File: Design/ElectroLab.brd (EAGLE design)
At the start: 175 x 100 mm, 232 parts, among them IC1 LM2902DT, IC10 CD4511BNSR, IC11 PAM8403, IC13 ADXL337, IC14 MIC5205, IC2 LM2902DT, IC3 SN74LV08ADR, IC4 SN74LV32ADR, IC5 SN74LV04ADR, IC6 4027D, IC7 4027D, IC8 NE555D, U1 USB, U2 GAS_SENSOR

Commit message: Updated V3R1
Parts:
- removed AR1, AR2, AR3, AR4: 1K, SpaceDIY:RESISTOR_ARRAY_X8_CAY17
- removed C33, C34: 10uF, SpaceDIY_passive_components:0603
- removed D1, D2, D3, D4: (no value), Seeed-OPL-Diode:LED-1206
- removed DP1: 2X7_SEGMENT_COMMON_CATODE_12_PINS, SpaceDIY:2X7_SEGMENT_COMMON_CATODE_12_PINS
- removed IC1, IC2: LM2902DT, Texas Instruments_By_element14_Batch_1:SOIC127P600X175-14N
- removed IC10: CD4511BNSR, SpaceDIY:SN74LS247D
- removed IC5: SN74LV04ADR, Texas Instruments_By_element14_Batch_1:SOIC127P600X175-14N
- removed JC1, JC2: SWTCHCRFT_3.5JACK5-JACK-SMD, jmsaavedra:4-JACK-SMD
- removed L0, L1, L2, L3, L4, L5, L6, L7: (no value), adafruit:1206
- removed L10, L17, L8, L9: Grn, adafruit:1206
- removed L11, L12, L13: Ylw, adafruit:1206
- removed L14, L15, L16: Red, adafruit:1206
- removed LDR: (no value), photo-elements:TO-5_V10
- removed LED_: (no value), SpaceDIY_passive_components:PLCC-6
- removed PB1, PB2, PB3, PB4, PB5, PB6, PB7, PB8, PB9: (no value), Seeed-OPL-Switch:SW4-SMD-6.0X6.0X5.0MM
- removed PH10, PH2, PH21, PH3, PH4, PH5, PH6, PH7, PH8, PH9: (no value), pinhead:1X02
- removed PH11, PH14, PH15, PH16, PH17, PH18, PH19, PH20, PH22, PH23, PH24, PH25, PH26, PH27, PH28, PH29, PH30, PH38, PH64: (no value), pinhead:1X03
- removed PH31, PH58, PH59, PH60, PH61, PH62: (no value), pinhead:1X30
- removed PH32, PH33, PH35, PH36, PH37, PH65: (no value), pinhead:1X04
- removed PH34: (no value), pinhead:1X01
- removed PH39, PH40: (no value), pinhead:1X06
- removed PH41: (no value), pinhead:2X07
- removed PH42, PH43, PH44, PH45, PH46: (no value), pinhead:1X08
- removed PH47: (no value), pinhead:1X09
- removed PH48, PH49, PH50, PH51, PH52, PH53, PH54, PH55, PH56, PH57: (no value), adafruit:1X10-BIG
- removed PH63: (no value), con-lstb:MA08-2
- added ARR1, ARR2, ARR3, ARR4, ARR5, ARR6, ARR7: 4_RES_ARRAY_R06031KOHM, SpaceDIY_passive_components:0603-ARC
- added C28, C37, C38, C39: 10uF, rcl:C0603
- added D5, D6, D7, D8: LL4148, SpaceDIY_semiconductors:LL-34
- added IC15: 74HC32S14-13, SpaceDIY_IC:SO14
- added IC9: TP4056, TP4056:SOT23-8
- added J1: (no value), SpaceDIY_connectors:JST-2-SMD
- added J10, J11, J12, J2, J4, J5, J6, J7, J8, J9: (no value), SpaceDIY_connectors:1X10
- added J13: AUDIO_JACK_MONO_3.5LCSC, SpaceDIY_connectors:PJ316
- added J14, J15, J16, J17, J18, J19: (no value), SpaceDIY_connectors:1X30
- added J20, J21, J22, J23, J24, J25, J26, J27, J28, J29, J30, J31, J32, J33, J34, J35, J36, J37: (no value), SpaceDIY_connectors:1X03
- added J3, J43, J44, J52, J53, J55: (no value), SpaceDIY_connectors:1X04
- added J38, J39, J40, J41, J47, J48, J49, J50, J54: (no value), SpaceDIY_connectors:1X02
- added J42, J51: (no value), SpaceDIY_connectors:1X01
- added J45, J46: (no value), SpaceDIY_connectors:1X06
- added J56: (no value), SpaceDIY_connectors:1X09
- added LED1, LED10, LED11, LED12, LED13, LED2, LED3, LED4, LED5, LED6, LED7, LED8, LED9: E6CC1205RYGC2UDA, SpaceDIY_semiconductors:BICOLOR_LED
- added RGB: CLEAR, SpaceDIY_semiconductors:LED-RGB-THRU
- added S10, S2, S3, S4, S5, S6, S7, S8, S9: MOMENTARY-SWITCH-SPST-PTH-6.0MM, SparkFun-Switches:TACTILE_SWITCH_PTH_6.0MM
- added U$1: FJ5101AG, SpaceDIY_semiconductors:7-SEGMENT
- added U$2, U$3, U$4, U$5, U$6: CONN_08, SpaceDIY_connectors:1X08
- added U$7: CD4511BNSR, SpaceDIY_IC:SO16
- added U3: AMS1117-3.3VSMD, SpaceDIY_IC:SOT223
- added X8: USB-C-POWER, SpaceDIY_connectors:USB-C-POWER
- C1, C10, C11, C12, C13, C14, C15, C16, C2, C3, C4, C5, C6, C7, C8, C9: device resistor:C1206 -> SpaceDIY_passive_components:0603
- C17, C18: device rcl:A/3216-18R -> SpaceDIY_passive_components:B/3528-21R
- C19, C20, C35, C36: device rcl:D/7343-31R -> SpaceDIY_passive_components:D/7343-31R
- C27: device rcl:D/7343-31W -> SpaceDIY_passive_components:D/7343-31R
- C29, C30, C31: value 10nF -> 0.1uF
- C32: value 100nF -> 0.1uF
- H1, H2, H3, H4: value (none) -> MOUNT-PAD-ROUND2.8
- IC13: value ADXL337 -> 74HC08DD; device SpaceDIY_IC:LFCSP-3X3 -> SpaceDIY_IC:SO14
- IC14: value MIC5205 -> 74HC04DD; device SparkFun:SOT23-5 -> SpaceDIY_IC:SO14
- IC3: value SN74LV08ADR -> LM324DTD; device Texas Instruments_By_element14_Batch_1:SOIC127P600X175-14N -> SpaceDIY_IC:SO14
- IC4: value SN74LV32ADR -> LM324DTD; device Texas Instruments_By_element14_Batch_1:SOIC127P600X175-14N -> SpaceDIY_IC:SO14
- IC6, IC7: value 4027D -> MC74HC112ADR2G; device 40xx:SO16 -> SpaceDIY_IC:SO16
- IC8: value NE555D -> TLC555CDR
- MIC: value ELECTRET_MICROPHON-WM-64PC/64PK -> MICROPHONE; device microphon:WM-64PC/64PK -> SpaceDIY_sensors:MICROPHONE
- NTC: device adafruit:R1206@1 -> SpaceDIY_sensors:NTC
- P1: value (none) -> SLIDE_POT_20MM; device SpaceDIY:SLIDE_POT_20MM -> SpaceDIY_electromechanical:RS201111J011
- PH1: value (none) -> PHOTORESISTOR; device pinhead:1X01 -> SpaceDIY_sensors:GL5516
- PH12: device pinhead:1X03 -> SpaceDIY_connectors:1X03
- R1, R10, R11, R12, R13, R14, R15, R16, R17, R18, R19, R2, R20, R21, R22, R23, R24, R25, R26, R27, R28, R29, R3, R30, R31, R35, R36, R37, R38, R39, R4, R41, R42, R43, R44, R45, R46, R47, R48, R49, R5, R50, R51, R52, R53, R54, R55, R56, R57, R58, R59, R6, R7, R8, R9: device resistor:R1206 -> SpaceDIY_passive_components:0603
- R32: value 330 -> 1.2k; device resistor:R1206 -> rcl:R0603
- R33: value 330 -> 1K; device resistor:R1206 -> SpaceDIY_passive_components:0603
- R34: value 330 -> 1k; device resistor:R1206 -> SpaceDIY_passive_components:0603
- SP1: value 32MM_SPEAKER -> SPEAKERFS1508MB0810-H8.0; device SpaceDIY:32MM_SPEAKER -> SpaceDIY_electromechanical:FS1508MB0810-H8.0
- T1: value (none) -> MMBT2222A; device transistor:SOT23-BEC -> SpaceDIY_semiconductors:SOT23
- T2, T3: value (none) -> T_NPNMMBT2222A-1P_CHANGJ_SOT23-BEC; device transistor:SOT23-BEC -> SpaceDIY_semiconductors:SOT23
- T4, T5: value (none) -> T_PNPMMBT5401_CHANGJ_SOT23-BEC; device transistor:SOT23-BCE -> SpaceDIY_semiconductors:SOT23
- U$16: device SpaceDIY:RESISTIVE_SENSOR_PAD -> SpaceDIY_sensors:RESISTIVE_SENSOR_PAD
- U1: value USB -> ADXL335; device daspilker:FCI-10103594-0001LF -> SparkFun-Sensors:LFCSP-16-4X4
- U2: device SparkFun:MQ-3 -> SpaceDIY_sensors:GAS_SENSOR
- moved U1 112.9 mm to (116.8, 47.0), flipped to the bottom, turned to 0 degrees
- moved PH1 102.9 mm to (73.7, 47.0), turned to 270 degrees
- moved R37 74.5 mm to (89.6, 74.3), turned to 90 degrees
- moved R36 71.6 mm to (86.7, 74.3), turned to 90 degrees
- moved R38 70.0 mm to (82.5, 49.6), turned to 270 degrees
- moved R35 68.9 mm to (83.8, 74.3), turned to 90 degrees
- moved IC14 51.0 mm to (167.5, 50.5), turned to 270 degrees
- moved R34 27.5 mm to (40.9, 92.1)
- moved R33 27.3 mm to (40.9, 95.1)
- moved IC4 26.4 mm to (162.0, 70.5), turned to 180 degrees
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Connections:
- removed net 3.3V: C32.1, C33.1, IC13.14, IC13.15, IC14.5
- removed net D0: PH41.1, PH63.1, R32.2
- removed net D1: PH41.2, PH63.2
- removed net D10: PH41.11, PH63.11, R37.2
- removed net D11: PH41.12, PH63.12
- removed net D12: PH41.13, PH63.13, R38.2
- removed net D13: PH41.14, PH63.14
- removed net D2: PH41.3, PH63.3, R33.2
- removed net D3: PH41.4, PH63.4
- removed net D4: PH41.5, PH63.5, R34.2
- removed net D5: PH41.6, PH63.6
- removed net D6: PH41.7, PH63.7, R35.2
- removed net D7: PH41.8, PH63.8
- removed net D8: PH41.9, PH63.9, R36.2
- removed net D9: PH41.10, PH63.10
- removed net DG1: DP1.9, PH3.1
- removed net DG2: DP1.4, PH3.2
- removed net DP: DP1.2
- removed net JC1: JC1.2, PH12.2
- removed net JC2: JC2.2, PH64.2
- removed net N$121: JC2.3, PH64.1
- removed net N$228: PB1.1, PB1.2, PB2.1, PB2.2, PB3.1, PB3.2, PH19.3
- removed net N$229: PB4.1, PB4.2, PB5.1, PB5.2, PB6.1, PB6.2, PH19.2
- removed net N$230: PB7.1, PB7.2, PB8.1, PB8.2, PB9.1, PB9.2, PH19.1
- removed net N$233: PB3.3, PB3.4, PB6.3, PB6.4, PB9.3, PB9.4, PH20.3
- removed net N$292: L8.A, R48.1
- removed net N$300: L9.A, R49.1
- removed net N$301: L10.A, R50.1
- removed net N$302: L11.A, R51.1
- removed net N$303: L12.A, R52.1
- removed net N$304: L13.A, R53.1
- removed net N$305: L14.A, R54.1
- removed net N$306: L15.A, R55.1
- removed net N$307: L16.A, R56.1
- removed net VEXT: PH63.15, S1.1
- removed net VUSB: S1.3, U1.1
- new net N$182: LED5.1, R49.2
- new net N$185: LED6.1, R50.2
- new net N$204: LED7.1, R51.2
- new net N$214: LED8.1, R52.2
- new net N$215: LED9.1, R53.2
- new net N$216: LED7.4, R35.2
- new net N$246: LED8.4, R36.2
- new net N$247: LED9.4, R37.2
- new net N$248: LED10.4, R54.2
- new net N$251: LED11.4, R55.2
- new net N$252: LED12.4, R56.2
- new net N$253: J20.3, S2.1, S3.1, S4.1
- new net N$258: J20.2, S5.1, S6.1, S7.1
- new net N$260: J21.3, S10.3, S4.3, S7.3
- new net N$261: J20.1, S10.1, S8.1, S9.1
- new net VBAT: C28.1, IC9.5, J1.1, S1.4
- new net VIN: C37.1, IC9.4, IC9.8, LED1.2, LED1.3, R38.2, U2.A1, U2.HA, X8.VBUS
- new net VOUT: C39.1, F1.2, U3.2
- net A1A: now also ARR1.1, IC13.1, U$2.1; no longer AR1.9, IC3.1, PH45.1
- net A1B: now also ARR1.2, IC13.2, U$2.2; no longer AR1.8, IC3.2, PH45.2
- net A1Y: now also IC13.3, J52.1; no longer IC3.3, PH36.1
- net A2A: now also ARR1.3, IC13.4, U$2.3; no longer AR1.7, IC3.4, PH45.3
- net A2B: now also ARR1.4, IC13.5, U$2.4; no longer AR1.6, IC3.5, PH45.4
- net A2Y: now also IC13.6, J52.2; no longer IC3.6, PH36.2
- net A3A: now also ARR2.1, IC13.9, U$2.5; no longer AR1.1, IC3.9, PH45.5
- net A3B: now also ARR2.2, IC13.10, U$2.6; no longer AR1.2, IC3.10, PH45.6
- net A3Y: now also IC13.8, J52.3; no longer IC3.8, PH36.3
- net A4A: now also ARR2.3, IC13.12, U$2.7; no longer AR1.3, IC3.12, PH45.7
- net A4B: now also ARR2.4, IC13.13, U$2.8; no longer AR1.4, IC3.13, PH45.8
- net A4Y: now also IC13.11, J52.4; no longer IC3.11, PH36.4
- net B: now also J37.3; no longer PH11.3
- net G: now also J37.2, R58.2; no longer PH11.2, R57.2
- net GND: now also ARR1.5, ARR1.6, ARR1.7, ARR1.8, ARR2.5, ARR2.6, ARR2.7, ARR2.8, ARR3.5, ARR3.6, ARR3.7, ARR3.8, ARR4.5, ARR4.6, ARR4.7, ARR4.8, ARR5.5, ARR5.6, ARR5.7, ARR5.8, ARR6.7, ARR6.8, ARR7.5, ARR7.6, ARR7.7, ARR7.8, C28.2, C37.2, C38.2, C39.2, IC14.7, IC15.7, IC3.11, IC4.11, IC6.10, IC6.14, IC6.15, IC7.10, IC7.14, IC7.15, IC9.1, IC9.3, J1.2, J14.1, J14.10, J14.11, J14.12, J14.13, J14.14, J14.15, J14.16, J14.17, J14.18, J14.19, J14.2, J14.20, J14.21, J14.22, J14.23, J14.24, J14.25, J14.26, J14.27, J14.28, J14.29, J14.3, J14.30, J14.4, J14.5, J14.6, J14.7, J14.8, J14.9, J36.1, LED13.1, LED2.1, LED3.1, R32.1, R35.1, R36.1, R37.1, R48.1, R49.1, R50.1, R51.1, R52.1, R53.1, R54.1, R55.1, R56.1, RGB.C, U$1.3, U$1.8, U$7.5, U$7.8, U1.3, U1.6, U1.7, U3.1, X8.GND; no longer AR1.10, AR1.5, AR2.10, AR2.5, AR3.10, AR3.5, AR4.10, AR4.5, C33.2, C34.2, IC1.11, IC10.GND, IC10.RBI, IC13.6, IC14.2, IC2.11, IC3.7, IC4.7, IC5.7, IC6.12, IC6.7, IC6.9, IC7.12, IC7.7, IC7.9, L0.C, L1.C, L10.C, L11.C, L12.C, L13.C, L14.C, L15.C, L16.C, L17.C, L2.C, L3.C, L4.C, L5.C, L6.C, L7.C, L8.C, L9.C, LED_.4, LED_.5, LED_.6, PH38.1, PH62.1, PH62.10, PH62.11, PH62.12, PH62.13, PH62.14, PH62.15, PH62.16, PH62.17, PH62.18, PH62.19, PH62.2, PH62.20, PH62.21, PH62.22, PH62.23, PH62.24, PH62.25, PH62.26, PH62.27, PH62.28, PH62.29, PH62.3, PH62.30, PH62.4, PH62.5, PH62.6, PH62.7, PH62.8, PH62.9, PH63.16
- net I1A: now also ARR5.1, IC14.1, J45.1; no longer AR3.9, IC5.1, PH39.1
- net I1Y: now also IC14.2, J46.1; no longer IC5.2, PH40.1
- net I2A: now also ARR5.2, IC14.3, J45.2; no longer AR3.3, IC5.3, PH39.2
- net I2Y: now also IC14.4, J46.2; no longer IC5.4, PH40.2
- net I3A: now also ARR5.3, IC14.5, J45.3; no longer AR3.7, IC5.5, PH39.3
- net I3Y: now also IC14.6, J46.3; no longer IC5.6, PH40.3
- net I4A: now also ARR5.4, IC14.9, J45.4; no longer AR3.6, IC5.9, PH39.4
- net I4Y: now also IC14.8, J46.4; no longer IC5.8, PH40.4
- net I5A: now also ARR6.1, IC14.11, J45.5; no longer AR3.1, IC5.11, PH39.5
- net I5Y: now also IC14.10, J46.5; no longer IC5.10, PH40.5
- net I6A: now also ARR6.2, IC14.13, J45.6; no longer AR3.2, IC5.13, PH39.6
- net I6Y: now also IC14.12, J46.6; no longer IC5.12, PH40.6
- net IA: now also ARR7.1, J55.1, U$7.7; no longer AR4.9, IC10.IA, PH35.1
- net IB: now also ARR7.2, J55.2, U$7.1; no longer AR4.8, IC10.IB, PH35.2
- net IC: now also ARR7.3, J55.3, U$7.2; no longer AR4.7, IC10.IC, PH35.3
- net ID: now also ARR7.4, J55.4, U$7.6; no longer AR4.6, IC10.ID, PH35.4
- net IN_L: now also J36.3; no longer PH38.3
- net IN_R: now also J36.2; no longer PH38.2
- net L1: now also J56.1, LED4.2; no longer PH47.9, R48.2
- net L2: now also J56.2, LED5.2; no longer PH47.8, R49.2
- net L3: now also J56.3, LED6.2; no longer PH47.7, R50.2
- net L4: now also J56.4, LED7.2, LED7.3; no longer PH47.6, R51.2
- net L5: now also J56.5, LED8.2, LED8.3; no longer PH47.5, R52.2
- net L6: now also J56.6, LED9.2, LED9.3; no longer PH47.4, R53.2
- net L7: now also J56.7, LED10.3; no longer PH47.3, R54.2
- net L8: now also J56.8, LED11.3; no longer PH47.2, R55.2
- net L9: now also J56.9, LED12.3; no longer PH47.1, R56.2
- net N$1: now also J2.1; no longer PH48.10
- net N$10: now also J2.10; no longer PH48.1
- net N$100: now also J12.1; no longer PH55.1
- net N$101: now also D8.A, J53.4; no longer D4.+, PH32.4
- net N$102: now also J13.2, PH12.2; no longer L1.A, R32.1
- net N$103: now also LED2.2; no longer L0.A
- net N$104: now also IC9.6, R34.2; no longer L2.A, R33.1
- net N$105: now also LED1.4, R33.1; no longer L3.A, R34.1
- net N$106: now also LED1.1, R34.1; no longer L4.A, R35.1
- net N$107: now also IC9.2, R32.2; no longer L5.A, R36.1
- net N$108: now also IC9.7, R33.2; no longer L6.A, R37.1
- net N$109: now also C38.1, S1.5, U3.3; no longer L7.A, R38.1
- net N$11: now also J4.10; no longer PH49.10
- net N$110: now also D8.C, J44.4; no longer D4.-, PH33.4
- net N$111: now also D5.A, J53.1; no longer D1.+, PH32.1
- net N$112: now also IC6.5, J47.1; no longer IC6.1, PH9.2
- net N$113: now also IC6.9, J48.1; no longer IC6.15, PH7.2
- net N$114: now also IC7.5, J49.1; no longer IC7.1, PH10.2
- net N$115: now also IC7.9, J50.1; no longer IC7.15, PH8.2
- net N$116: now also J13.1; no longer JC1.3
- net N$117: now also RGB.G; no longer LED_.2
- net N$118: now also LED4.1, R48.2; no longer F1.1, S1.2
- net N$119: now also J42.1; no longer PH34.1
- net N$12: now also J4.9; no longer PH49.9
- net N$120: now also LED13.2, R38.1; no longer JC2.1, PH64.3
- net N$122: now also LED3.2; no longer L17.A
- net N$125: now also J41.2; no longer PH21.1
- net N$126: now also J41.1; no longer PH21.2
- net N$127: now also J15.24, J16.24, J17.24, J18.24; no longer PH31.7, PH59.7, PH60.7, PH61.7
- net N$128: now also J15.30, J16.30, J17.30, J18.30; no longer PH31.1, PH59.1, PH60.1, PH61.1
- net N$129: now also J15.29, J16.29, J17.29, J18.29; no longer PH31.2, PH59.2, PH60.2, PH61.2
- net N$13: now also J4.8; no longer PH49.8
- net N$130: now also IC3.3, U$4.1; no longer IC1.13, PH42.1
- net N$131: now also IC3.2, U$4.2; no longer IC1.12, PH42.2
- net N$132: now also IC3.5, U$4.3; no longer IC1.9, PH42.3
- net N$133: now also IC3.6, U$4.4; no longer IC1.10, PH42.4
- net N$134: now also IC3.10, U$4.5; no longer IC1.6, PH42.5
- net N$135: now also IC3.9, U$4.6; no longer IC1.5, PH42.6
- net N$136: now also IC3.12, U$4.7; no longer IC1.2, PH42.7
- net N$137: now also IC3.13, U$4.8; no longer IC1.3, PH42.8
- net N$138: now also IC4.3, U$5.1; no longer IC2.13, PH43.1
- net N$139: now also J15.28, J16.28, J17.28, J18.28; no longer PH31.3, PH59.3, PH60.3, PH61.3
- net N$14: now also J4.7; no longer PH49.7
- net N$140: now also J15.27, J16.27, J17.27, J18.27; no longer PH31.4, PH59.4, PH60.4, PH61.4
- net N$141: now also J15.26, J16.26, J17.26, J18.26; no longer PH31.5, PH59.5, PH60.5, PH61.5
- net N$142: now also J15.25, J16.25, J17.25, J18.25; no longer PH31.6, PH59.6, PH60.6, PH61.6
- net N$143: now also J15.23, J16.23, J17.23, J18.23; no longer PH31.8, PH59.8, PH60.8, PH61.8
- net N$144: now also J15.22, J16.22, J17.22, J18.22; no longer PH31.9, PH59.9, PH60.9, PH61.9
- net N$145: now also J15.21, J16.21, J17.21, J18.21; no longer PH31.10, PH59.10, PH60.10, PH61.10
- net N$146: now also IC6.2, J26.1; no longer IC6.5, PH27.1
- net N$147: now also J15.20, J16.20, J17.20, J18.20; no longer PH31.11, PH59.11, PH60.11, PH61.11
- net N$148: now also J15.19, J16.19, J17.19, J18.19; no longer PH31.12, PH59.12, PH60.12, PH61.12
- net N$149: now also J15.18, J16.18, J17.18, J18.18; no longer PH31.13, PH59.13, PH60.13, PH61.13
- net N$15: now also J4.5; no longer PH49.5
- net N$150: now also J15.17, J16.17, J17.17, J18.17; no longer PH31.14, PH59.14, PH60.14, PH61.14
- net N$151: now also J15.16, J16.16, J17.16, J18.16; no longer PH31.15, PH59.15, PH60.15, PH61.15
- net N$152: now also J15.15, J16.15, J17.15, J18.15; no longer PH31.16, PH59.16, PH60.16, PH61.16
- net N$153: now also J15.14, J16.14, J17.14, J18.14; no longer PH31.17, PH59.17, PH60.17, PH61.17
- net N$154: now also J15.13, J16.13, J17.13, J18.13; no longer PH31.18, PH59.18, PH60.18, PH61.18
- net N$155: now also IC6.1, J26.2; no longer IC6.3, PH27.2
- net N$156: now also IC6.3, J26.3; no longer IC6.6, PH27.3
- net N$157: now also IC6.12, J27.1; no longer IC6.11, PH25.1
- net N$158: now also J27.2; no longer PH25.2
- net N$159: now also IC6.11, J27.3; no longer IC6.10, PH25.3
- net N$16: now also J4.6; no longer PH49.6
- net N$160: now also IC7.2, J28.1; no longer IC7.5, PH28.1
- net N$161: now also IC7.1, J28.2; no longer IC7.3, PH28.2
- net N$162: now also IC7.3, J28.3; no longer IC7.6, PH28.3
- net N$163: now also J15.12, J16.12, J17.12, J18.12; no longer PH31.19, PH59.19, PH60.19, PH61.19
- net N$164: now also J15.11, J16.11, J17.11, J18.11; no longer PH31.20, PH59.20, PH60.20, PH61.20
- net N$165: now also J15.10, J16.10, J17.10, J18.10; no longer PH31.21, PH59.21, PH60.21, PH61.21
- net N$166: now also J15.9, J16.9, J17.9, J18.9; no longer PH31.22, PH59.22, PH60.22, PH61.22
- net N$167: now also J15.8, J16.8, J17.8, J18.8; no longer PH31.23, PH59.23, PH60.23, PH61.23
- net N$168: now also J15.7, J16.7, J17.7, J18.7; no longer PH31.24, PH59.24, PH60.24, PH61.24
- net N$169: now also J15.6, J16.6, J17.6, J18.6; no longer PH31.25, PH59.25, PH60.25, PH61.25
- net N$17: now also J4.4; no longer PH49.4
- net N$170: now also J15.5, J16.5, J17.5, J18.5; no longer PH31.26, PH59.26, PH60.26, PH61.26
- net N$171: now also IC7.12, J29.1; no longer IC7.11, PH26.1
- net N$172: now also J29.2; no longer PH26.2
- net N$173: now also IC7.11, J29.3; no longer IC7.10, PH26.3
- net N$174: now also J15.4, J16.4, J17.4, J18.4; no longer PH31.27, PH59.27, PH60.27, PH61.27
- net N$175: now also J15.3, J16.3, J17.3, J18.3; no longer PH31.28, PH59.28, PH60.28, PH61.28
- net N$176: now also J15.2, J16.2, J17.2, J18.2; no longer PH31.29, PH59.29, PH60.29, PH61.29
- net N$177: now also J15.1, J16.1, J17.1, J18.1; no longer PH31.30, PH59.30, PH60.30, PH61.30
- net N$178: now also IC6.6, J47.2; no longer IC6.2, PH9.1
- net N$179: now also IC6.7, J48.2; no longer IC6.14, PH7.1
- net N$18: now also J4.3; no longer PH49.3
- net N$180: now also IC7.6, J49.2; no longer IC7.2, PH10.1
- net N$181: now also IC7.7, J50.2; no longer IC7.14, PH8.1
- net N$183: now also D7.A, J53.3; no longer D3.+, PH32.3
- net N$184: now also D6.A, J53.2; no longer D2.+, PH32.2
- net N$186: now also IC4.2, U$5.2; no longer IC2.12, PH43.2
- net N$187: now also IC4.5, U$5.3; no longer IC2.9, PH43.3
- net N$188: now also IC4.6, U$5.4; no longer IC2.10, PH43.4
- net N$189: now also IC4.10, U$5.5; no longer IC2.6, PH43.5
- net N$19: now also J4.2; no longer PH49.2
- net N$190: now also IC4.9, U$5.6; no longer IC2.5, PH43.6
- net N$191: now also IC4.12, U$5.7; no longer IC2.2, PH43.7
- net N$192: now also IC4.13, U$5.8; no longer IC2.3, PH43.8
- net N$193: now also IC3.1, U$6.1; no longer IC1.14, PH44.8
- net N$194: now also IC3.7, U$6.2; no longer IC1.8, PH44.7
- net N$195: now also IC3.8, U$6.3; no longer IC1.7, PH44.6
- net N$196: now also IC3.14, U$6.4; no longer IC1.1, PH44.5
- net N$197: now also IC4.1, U$6.5; no longer IC2.14, PH44.4
- net N$198: now also IC4.7, U$6.6; no longer IC2.8, PH44.3
- net N$199: now also D5.C, J44.1; no longer D1.-, PH33.1
- net N$2: now also J2.2; no longer PH48.9
- net N$20: now also J4.1; no longer PH49.1
- net N$200: now also IC4.8, U$6.7; no longer IC2.7, PH44.2
- net N$201: now also IC4.14, U$6.8; no longer IC2.1, PH44.1
- net N$202: now also D6.C, J44.2; no longer D2.-, PH33.2
- net N$203: now also D7.C, J44.3; no longer D3.-, PH33.3
- net N$205: now also J31.1, T1.2; no longer PH16.1, T1.E
- net N$206: now also J31.2, T1.1; no longer PH16.2, T1.B
- net N$207: now also J31.3, T1.3; no longer PH16.3, T1.C
- net N$208: now also J32.1, T2.2; no longer PH17.1, T2.E
- net N$209: now also J32.2, T2.1; no longer PH17.2, T2.B
- net N$21: now also J5.1; no longer PH50.10
- net N$210: now also J32.3, T2.3; no longer PH17.3, T2.C
- net N$211: now also J33.1, T3.2; no longer PH18.1, T3.E
- net N$212: now also J33.2, T3.1; no longer PH18.2, T3.B
- net N$213: now also J33.3, T3.3; no longer PH18.3, T3.C
- net N$217: now also J34.1, T4.3; no longer PH14.1, T4.C
- net N$218: now also J34.2, T4.1; no longer PH14.2, T4.B
- net N$219: now also J34.3, T4.2; no longer PH14.3, T4.E
- net N$22: now also J5.2; no longer PH50.9
- net N$220: now also J35.1, T5.3; no longer PH15.1, T5.C
- net N$221: now also J35.2, T5.1; no longer PH15.2, T5.B
- net N$222: now also J35.3, T5.2; no longer PH15.3, T5.E
- net N$223: now also J30.1; no longer PH29.1
- net N$224: now also J51.1; no longer PH1.1
- net N$226: now also J30.2; no longer PH29.2
- net N$227: now also J30.3; no longer PH29.3
- net N$23: now also J5.3; no longer PH50.8
- net N$231: now also J21.1, S2.3, S5.3, S8.3; no longer PB1.3, PB1.4, PB4.3, PB4.4, PB7.3, PB7.4, PH20.1
- net N$232: now also J21.2, S3.3, S6.3, S9.3; no longer PB2.3, PB2.4, PB5.3, PB5.4, PB8.3, PB8.4, PH20.2
- net N$234: now also J39.1, PH1.1; no longer LDR.1, PH5.1
- net N$235: now also J39.2, PH1.3; no longer LDR.2, PH5.2
- net N$236: now also J40.1; no longer PH6.1
- net N$237: now also J23.1; no longer PH22.1
- net N$238: now also J23.2; no longer PH22.2
- net N$239: now also J23.3; no longer PH22.3
- net N$24: now also J5.4; no longer PH50.7
- net N$240: now also J22.1; no longer PH24.1
- net N$241: now also J22.2; no longer PH24.2
- net N$242: now also J22.3; no longer PH24.3
- net N$243: now also J24.1; no longer PH23.1
- net N$244: now also J24.2; no longer PH23.2
- net N$245: now also J24.3; no longer PH23.3
- net N$249: now also J38.1; no longer PH4.1
- net N$25: now also J5.5; no longer PH50.6
- net N$250: now also J38.2; no longer PH4.2
- net N$256: now also J40.2; no longer PH6.2
- net N$257: now also J54.2; no longer PH2.1
- net N$26: now also J5.6; no longer PH50.5
- net N$264: now also J13.3; no longer JC1.1
- net N$27: now also J5.7; no longer PH50.4
- net N$28: now also J5.8; no longer PH50.3
- net N$29: now also J5.9; no longer PH50.2
- net N$291: now also J54.1; no longer PH2.2
- net N$3: now also J2.3; no longer PH48.8
- net N$30: now also J5.10; no longer PH50.1
- net N$308: now also RGB.R; no longer LED_.1
- net N$31: now also J6.10; no longer PH51.10
- net N$310: now also RGB.B; no longer LED_.3
- net N$32: now also J6.9; no longer PH51.9
- net N$33: now also J6.8; no longer PH51.8
- net N$34: now also J6.7; no longer PH51.7
- net N$35: now also J6.6; no longer PH51.6
- net N$36: now also J6.5; no longer PH51.5
- net N$37: now also J6.4; no longer PH51.4
- net N$38: now also J6.3; no longer PH51.3
- net N$39: now also J6.2; no longer PH51.2
- net N$4: now also J2.4; no longer PH48.7
- net N$40: now also J6.1; no longer PH51.1
- net N$41: now also J7.1; no longer PH52.10
- net N$42: now also J7.2; no longer PH52.9
- net N$43: now also J7.3; no longer PH52.8
- net N$44: now also J7.4; no longer PH52.7
- net N$45: now also J7.5; no longer PH52.6
- net N$46: now also J7.6; no longer PH52.5
- net N$47: now also J7.7; no longer PH52.4
- net N$48: now also J7.8; no longer PH52.3
- net N$49: now also J7.9; no longer PH52.2
- net N$5: now also J2.5; no longer PH48.6
- net N$50: now also J7.10; no longer PH52.1
- net N$51: now also J8.10; no longer PH53.10
- net N$52: now also J8.9; no longer PH53.9
- net N$53: now also J8.8; no longer PH53.8
- net N$54: now also J8.7; no longer PH53.7
- net N$55: now also J8.6; no longer PH53.6
- net N$56: now also J8.5; no longer PH53.5
- net N$57: now also J8.4; no longer PH53.4
- net N$58: now also J8.3; no longer PH53.3
- net N$59: now also J8.2; no longer PH53.2
- net N$6: now also J2.6; no longer PH48.5
- net N$60: now also J8.1; no longer PH53.1
- net N$61: now also J9.1; no longer PH56.10
- net N$62: now also J9.2; no longer PH56.9
- net N$63: now also J9.3; no longer PH56.8
- net N$64: now also J9.4; no longer PH56.7
- net N$65: now also J9.5; no longer PH56.6
- net N$66: now also J9.6; no longer PH56.5
- net N$67: now also J9.7; no longer PH56.4
- net N$68: now also J9.8; no longer PH56.3
- net N$69: now also J9.9; no longer PH56.2
- net N$7: now also J2.7; no longer PH48.4
- net N$70: now also J9.10; no longer PH56.1
- net N$71: now also J10.1; no longer PH57.1
- net N$72: now also J10.2; no longer PH57.2
- net N$73: now also J10.3; no longer PH57.3
- net N$74: now also J10.4; no longer PH57.4
- net N$75: now also J10.5; no longer PH57.5
- net N$76: now also J10.6; no longer PH57.6
- net N$77: now also J10.7; no longer PH57.7
- net N$78: now also J10.8; no longer PH57.8
- net N$79: now also J10.9; no longer PH57.9
- net N$8: now also J2.8; no longer PH48.3
- net N$80: now also J10.10; no longer PH57.10
- net N$81: now also J11.1; no longer PH54.10
- net N$82: now also J11.2; no longer PH54.9
- net N$83: now also J11.3; no longer PH54.8
- net N$84: now also J11.4; no longer PH54.7
- net N$85: now also J11.5; no longer PH54.6
- net N$86: now also J11.6; no longer PH54.5
- net N$87: now also J11.7; no longer PH54.4
- net N$88: now also J11.8; no longer PH54.3
- net N$89: now also J11.9; no longer PH54.2
- net N$9: now also J2.9; no longer PH48.2
- net N$90: now also J11.10; no longer PH54.1
- net N$91: now also J12.10; no longer PH55.10
- net N$92: now also J12.9; no longer PH55.9
- net N$93: now also J12.8; no longer PH55.8
- net N$94: now also J12.7; no longer PH55.7
- net N$95: now also J12.6; no longer PH55.6
- net N$96: now also J12.5; no longer PH55.5
- net N$97: now also J12.4; no longer PH55.4
- net N$98: now also J12.3; no longer PH55.3
- net N$99: now also J12.2; no longer PH55.2
- net O1A: now also ARR3.1, IC15.1, U$3.1; no longer AR2.9, IC4.1, PH46.1
- net O1B: now also ARR3.2, IC15.2, U$3.2; no longer AR2.8, IC4.2, PH46.2
- net O1Y: now also IC15.3, J43.1; no longer IC4.3, PH37.1
- net O2A: now also ARR3.3, IC15.4, U$3.3; no longer AR2.7, IC4.4, PH46.3
- net O2B: now also ARR3.4, IC15.5, U$3.4; no longer AR2.6, IC4.5, PH46.4
- net O2Y: now also IC15.6, J43.2; no longer IC4.6, PH37.2
- net O3A: now also ARR4.1, IC15.9, U$3.5; no longer AR2.1, IC4.9, PH46.5
- net O3B: now also ARR4.2, IC15.10, U$3.6; no longer AR2.2, IC4.10, PH46.6
- net O3Y: now also IC15.8, J43.3; no longer IC4.8, PH37.3
- net O4A: now also ARR4.3, IC15.12, U$3.7; no longer AR2.3, IC4.12, PH46.7
- net O4B: now also ARR4.4, IC15.13, U$3.8; no longer AR2.4, IC4.13, PH46.8
- net O4Y: now also IC15.11, J43.4; no longer IC4.11, PH37.4
- net OUT_L+: now also J3.1; no longer PH65.4
- net OUT_L-: now also J3.2; no longer PH65.3
- net OUT_R+: now also J3.3; no longer PH65.2
- net OUT_R-: now also J3.4; no longer PH65.1
- net R: now also J37.1, R57.2; no longer PH11.1, R58.2
- net SA: now also U$1.7; no longer DP1.10
- net SA': now also U$7.13; no longer IC10.A
- net SB: now also U$1.6; no longer DP1.8
- net SB': now also U$7.12; no longer IC10.B
- net SC: now also U$1.4; no longer DP1.1
- net SC': now also U$7.11; no longer IC10.C
- net SD: now also U$1.2; no longer DP1.5
- net SD': now also U$7.10; no longer IC10.D
- net SE: now also U$1.1; no longer DP1.3
- net SE': now also U$7.9; no longer IC10.E
- net SF: now also U$1.9; no longer DP1.6
- net SF': now also U$7.15; no longer IC10.F
- net SG: now also U$1.10; no longer DP1.7
- net SG': now also U$7.14; no longer IC10.G
- net VCC: now also C32.1, F1.1, IC13.14, IC14.14, IC15.14, IC3.4, IC4.4, J19.1, J19.10, J19.11, J19.12, J19.13, J19.14, J19.15, J19.16, J19.17, J19.18, J19.19, J19.2, J19.20, J19.21, J19.22, J19.23, J19.24, J19.25, J19.26, J19.27, J19.28, J19.29, J19.3, J19.30, J19.4, J19.5, J19.6, J19.7, J19.8, J19.9, U$7.16, U$7.3, U$7.4, U1.14, U1.15; no longer C34.1, F1.2, IC1.4, IC10.BI/RBO, IC10.LT, IC10.VCC, IC14.1, IC14.3, IC2.4, IC3.14, IC4.14, IC5.14, PH58.1, PH58.10, PH58.11, PH58.12, PH58.13, PH58.14, PH58.15, PH58.16, PH58.17, PH58.18, PH58.19, PH58.2, PH58.20, PH58.21, PH58.22, PH58.23, PH58.24, PH58.25, PH58.26, PH58.27, PH58.28, PH58.29, PH58.3, PH58.30, PH58.4, PH58.5, PH58.6, PH58.7, PH58.8, PH58.9, U2.A1, U2.HA
- net X+: now also J25.1, U1.12; no longer IC13.5, PH30.1
- net Y+: now also J25.2, U1.10; no longer IC13.4, PH30.2
- net Z+: now also J25.3, U1.8; no longer IC13.16, PH30.3
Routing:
- net VIN: track 0.00 -> 177.3 mm, vias 0 -> 2
- net VCC: track 491.8 -> 412.6 mm, vias 14 -> 5
- net N$228: track 77.1 -> 0.00 mm
- net N$229: track 68.5 -> 0.00 mm
- net N$230: track 63.1 -> 0.00 mm
- net VEXT: track 62.0 -> 0.00 mm
- net N$253: track 0.00 -> 60.7 mm
- net N$258: track 0.00 -> 52.0 mm
- net N$261: track 0.00 -> 44.5 mm
- net VBAT: track 0.00 -> 43.7 mm, vias 0 -> 1
- net N$233: track 42.8 -> 0.00 mm
- net N$260: track 0.00 -> 40.7 mm
- net N$108: track 5.81 -> 40.0 mm, vias 1 -> 2
- net D12: track 33.0 -> 0.00 mm
- net IA: track 43.4 -> 11.8 mm, vias 2 -> 0
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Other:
- board text added: "JLCJLCJLCJLC"

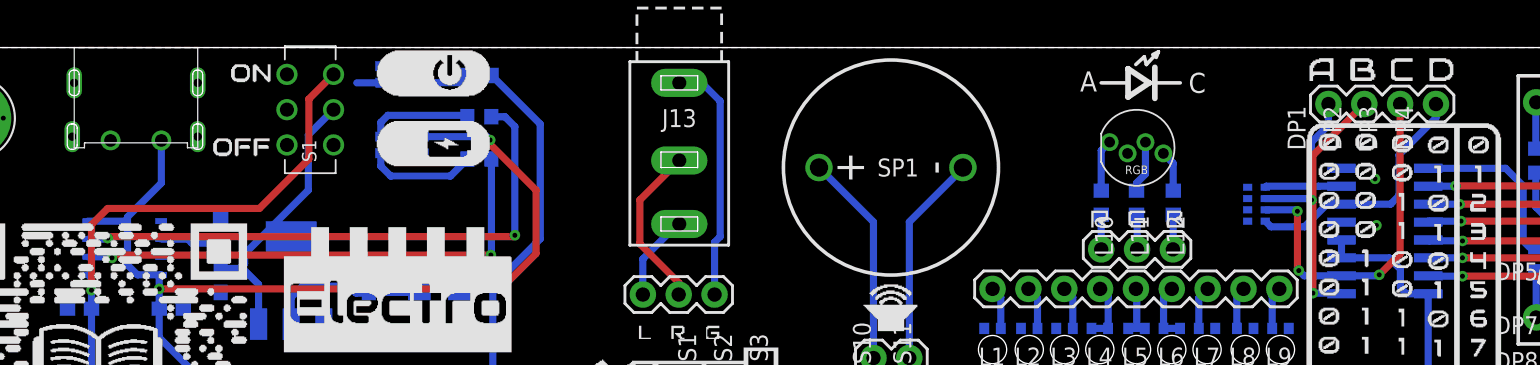
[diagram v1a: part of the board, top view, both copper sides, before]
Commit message: V3 fixed: - USB-C - BCD pinhead - 330 -> 470 Ohm on RED LEDs for orange led bards
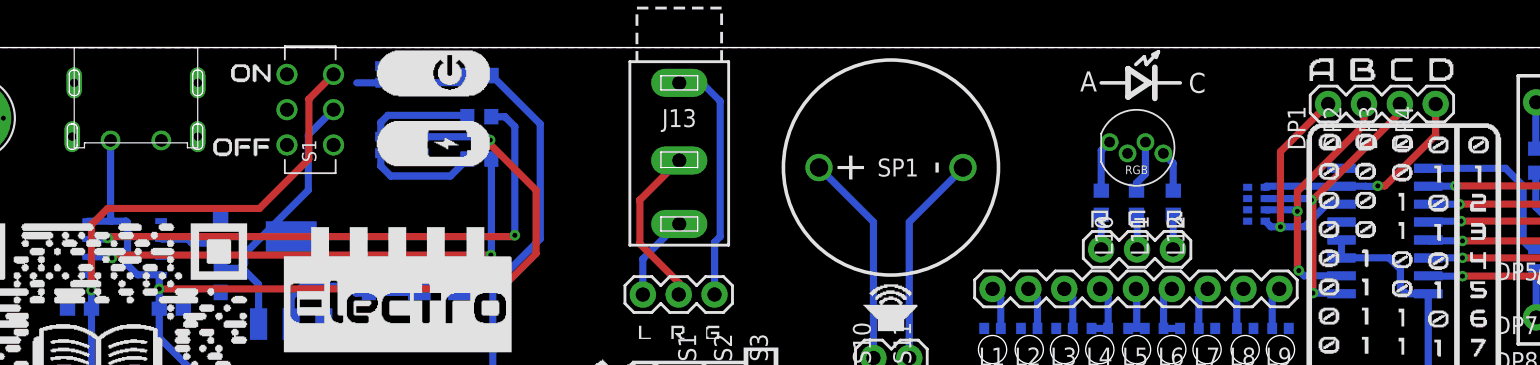
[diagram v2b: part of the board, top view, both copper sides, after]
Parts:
- R35, R36, R37: value 330 -> 470
- moved J55 7.60 mm to (108.6, 96.0), turned to 180 degrees
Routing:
- net IC: track 25.2 -> 19.3 mm, vias 3 -> 2
- net IA: track 11.8 -> 15.8 mm, vias 0 -> 1
- net ID: track 18.1 -> 16.3 mm, vias 0 -> 1
- net VIN: track 177.3 -> 176.3 mm
- net IB: track 20.4 -> 21.5 mm
- net GND: vias 18 -> 16
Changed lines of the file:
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@@
 <drawing>
 <settings>
-<setting alwaysvectorfont="yes"/>
+<setting alwaysvectorfont="no"/>
 <setting keepoldvectorfont="yes"/>
 <setting verticaltext="up"/>
 </settings>
-<grid distance="0.25" unitdist="mm" unit="mm" style="lines" multiple="1" display="yes" altdistance="0.025" altunitdist="inch" altunit="inch"/>
+<grid distance="0.1" unitdist="mm" unit="mm" style="lines" multiple="1" display="yes" altdistance="0.025" altunitdist="inch" altunit="inch"/>
 <layers>
 <layer number="1" name="Top" color="4" fill="1" visible="yes" active="yes"/>
@@
 <attribute name="VALUE" x="138.65" y="4.9" size="1.27" layer="28" rot="MR270" align="center"/>
 </element>
-<element name="X8" library="SpaceDIY_connectors" package="USB-C-POWER" value="USB-C-POWER" x="16.5" y="97.5" smashed="yes" rot="R180"/>
+<element name="X8" library="SpaceDIY_connectors" package="USB-C-POWER" value="USB-C-POWER" x="16.5" y="97.5" smashed="yes" rot="R180">
+<attribute name="LCSC" value="C2848624" x="16.5" y="97.5" size="1.778" layer="27" rot="R180" display="off"/>
+</element>
 <element name="IC9" library="TP4056" package="SOT23-8" value="TP4056" x="15.7" y="85.8" smashed="yes" rot="MR270">
 <attribute name="LCSC" value="C16581" x="15.7" y="85.8" size="1.778" layer="28" rot="MR270" display="off"/>
@@
 <attribute name="VALUE" x="72.57" y="80.032" size="0.6096" layer="27" font="vector" ratio="20" rot="R180"/>
 </element>
-<element name="J55" library="SpaceDIY_connectors" package="1X04" value="" x="101" y="96" smashed="yes">
-<attribute name="VALUE" x="99.73" y="93.968" size="0.6096" layer="27" font="vector" ratio="20"/>
+<element name="J55" library="SpaceDIY_connectors" package="1X04" value="" x="108.6" y="96" smashed="yes" rot="R180">
+<attribute name="VALUE" x="109.87" y="98.032" size="0.6096" layer="27" font="vector" ratio="20" rot="R180"/>
 </element>
 <element name="J56" library="SpaceDIY_connectors" package="1X09" value="" x="77.2" y="82.9" smashed="yes">
@@
 <attribute name="LCSC" value="C2802680" x="97.6" y="78.6" size="1.778" layer="28" rot="MR90" display="off"/>
 </element>
-<element name="R35" library="SpaceDIY_passive_components" package="0603" value="330" x="83.8" y="74.3" smashed="yes" rot="MR90">
+<element name="R35" library="SpaceDIY_passive_components" package="0603" value="470" x="83.8" y="74.3" smashed="yes" rot="MR90">
 <attribute name="VALUE" x="83.803" y="77.313" size="0.8" layer="28" rot="MR180" align="center"/>
 </element>
-<element name="R36" library="SpaceDIY_passive_components" package="0603" value="330" x="86.7" y="74.3" smashed="yes" rot="MR90">
+<element name="R36" library="SpaceDIY_passive_components" package="0603" value="470" x="86.7" y="74.3" smashed="yes" rot="MR90">
 <attribute name="VALUE" x="86.703" y="77.313" size="0.8" layer="28" rot="MR180" align="center"/>
 </element>
-<element name="R37" library="SpaceDIY_passive_components" package="0603" value="330" x="89.6" y="74.3" smashed="yes" rot="MR90">
+<element name="R37" library="SpaceDIY_passive_components" package="0603" value="470" x="89.6" y="74.3" smashed="yes" rot="MR90">
 <attribute name="VALUE" x="89.603" y="77.313" size="0.8" layer="28" rot="MR180" align="center"/>
 </element>
@@
 <wire x1="33.85" y1="97.515" x2="33.835" y2="97.5" width="0.508" layer="16"/>
 <wire x1="33.835" y1="97.5" x2="32.15" y2="97.5" width="0.508" layer="16"/>
-<via x="104.4" y="87.4" extent="1-16" drill="0.35"/>
-<via x="104.3" y="90.7" extent="1-16" drill="0.35"/>
 <wire x1="172.9" y1="11.585" x2="172.915" y2="11.6" width="0.508" layer="16"/>
 <wire x1="172.915" y1="11.6" x2="173.7" y2="11.6" width="0.508" layer="16"/>
@@
 <contactref element="ARR7" pad="1"/>
 <contactref element="U$7" pad="7"/>
-<wire x1="101" y1="96" x2="101" y2="94.5" width="0.508" layer="16"/>
-<wire x1="101" y1="94.5" x2="99.8" y2="93.3" width="0.508" layer="16"/>
-<wire x1="99.8" y1="93.3" x2="99.8" y2="90.3" width="0.508" layer="16"/>
-<wire x1="99.8" y1="90.3" x2="99.925" y2="90.175" width="0.508" layer="16"/>
-<wire x1="99.925" y1="90.175" x2="100.3" y2="90.175" width="0.508" layer="16"/>
-<wire x1="100.3" y1="90.175" x2="101.9266" y2="90.175" width="0.508" layer="16"/>
 <wire x1="96.525" y1="90.1" x2="96.6" y2="90.175" width="0.508" layer="16"/>
-<wire x1="99.925" y1="90.175" x2="96.6" y2="90.175" width="0.508" layer="16"/>
+<wire x1="101.9266" y1="90.175" x2="96.6" y2="90.175" width="0.508" layer="16"/>
+<via x="104.5" y="90.2" extent="1-16" drill="0.35"/>
+<wire x1="101.9266" y1="90.175" x2="103.64101875" y2="90.175" width="0.508" layer="16"/>
+<wire x1="103.64101875" y1="90.175" x2="103.65321875" y2="90.1628" width="0.508" layer="16"/>
+<wire x1="103.65321875" y1="90.1628" x2="104.4628" y2="90.1628" width="0.508" layer="16"/>
+<wire x1="104.5" y1="90.2" x2="104.4628" y2="90.1628" width="0.508" layer="16"/>
+<wire x1="108.6" y1="93.8" x2="105" y2="90.2" width="0.508" layer="1"/>
+<wire x1="104.5" y1="90.2" x2="105" y2="90.2" width="0.508" layer="1"/>
+<wire x1="108.6" y1="93.8" x2="108.6" y2="96" width="0.508" layer="1"/>
 </signal>
 <signal name="IB">
@@
 <wire x1="99.9" y1="82.6" x2="101.8816" y2="82.6" width="0.508" layer="16"/>
 <wire x1="101.8816" y1="82.6" x2="101.9266" y2="82.555" width="0.508" layer="16"/>
-<wire x1="103.54" y1="96" x2="99.9" y2="92.36" width="0.508" layer="1"/>
-<wire x1="99.9" y1="92.36" x2="99.9" y2="89.1" width="0.508" layer="1"/>
+<wire x1="99.8" y1="89.2" x2="99.9" y2="89.2" width="0.508" layer="1"/>
+<wire x1="106.06" y1="95.36" x2="106.06" y2="96" width="0.508" layer="1"/>
+<wire x1="99.9" y1="89.2" x2="106.06" y2="95.36" width="0.508" layer="1"/>
 </signal>
 <signal name="IC">
@@
 <wire x1="98.9" y1="84.2" x2="99.275" y2="83.825" width="0.508" layer="16"/>
 <wire x1="99.275" y1="83.825" x2="101.9266" y2="83.825" width="0.508" layer="16"/>
-<wire x1="101.9266" y1="83.825" x2="104.525" y2="83.825" width="0.508" layer="16"/>
-<wire x1="104.525" y1="83.825" x2="104.6" y2="83.9" width="0.508" layer="16"/>
-<via x="104.6" y="83.9" extent="1-16" drill="0.35"/>
-<wire x1="104.6" y1="83.9" x2="106.08" y2="85.38" width="0.508" layer="1"/>
-<wire x1="106.08" y1="85.38" x2="106.08" y2="96" width="0.508" layer="1"/>
+<wire x1="103.52" y1="96" x2="103.52" y2="94.52" width="0.508" layer="1"/>
+<wire x1="98.8" y1="89.8" x2="98.8" y2="88.4" width="0.508" layer="1"/>
+<wire x1="103.52" y1="94.52" x2="98.8" y2="89.8" width="0.508" layer="1"/>
 </signal>
 <signal name="ID">
@@
 <wire x1="96.925" y1="87.3" x2="96.525" y2="87.7" width="0.508" layer="16"/>
 <wire x1="100.905" y1="88.905" x2="99.3" y2="87.3" width="0.508" layer="16"/>
-<wire x1="99.3" y1="87.3" x2="96.925" y2="87.3" width="0.508" layer="16"/>
-<wire x1="101.9266" y1="88.905" x2="105.405" y2="88.905" width="0.508" layer="16"/>
-<wire x1="105.405" y1="88.905" x2="106" y2="89.5" width="0.508" layer="16"/>
-<wire x1="106" y1="89.5" x2="106" y2="92.4" width="0.508" layer="16"/>
-<wire x1="108.62" y1="95.02" x2="108.62" y2="96" width="0.508" layer="16"/>
-<wire x1="106" y1="92.4" x2="108.62" y2="95.02" width="0.508" layer="16"/>
+<wire x1="99.3" y1="87.3" x2="97.6" y2="87.3" width="0.508" layer="16"/>
+<wire x1="97.6" y1="87.3" x2="96.925" y2="87.3" width="0.508" layer="16"/>
+<wire x1="100.98" y1="96" x2="97.6" y2="92.62" width="0.508" layer="1"/>
+<wire x1="97.6" y1="92.62" x2="97.6" y2="87.3" width="0.508" layer="1"/>
+<via x="97.6" y="87.3" extent="1-16" drill="0.35"/>
 </signal>
 <signal name="SG">
@@
 <wire x1="16.605" y1="83.895" x2="15.9" y2="84.6" width="0.508" layer="16"/>
 <wire x1="15.9" y1="84.6" x2="15.9" y2="87.6" width="0.508" layer="16"/>
-<wire x1="15.9" y1="87.6" x2="15.9" y2="88" width="0.508" layer="16"/>
-<wire x1="15.9" y1="88" x2="18.3" y2="90.4" width="0.508" layer="16"/>
-<wire x1="18.3" y1="90.4" x2="18.3" y2="93.42" width="0.508" layer="16"/>
-<wire x1="13.12" y1="87.705" x2="15.795" y2="87.705" width="0.508" layer="16"/>
+<wire x1="13.12" y1="87.705" x2="14.75" y2="87.705" width="0.508" layer="16"/>
+<wire x1="14.75" y1="87.705" x2="15.795" y2="87.705" width="0.508" layer="16"/>
 <wire x1="15.795" y1="87.705" x2="15.9" y2="87.6" width="0.508" layer="16"/>
 <wire x1="36.85" y1="92.515" x2="36.85" y2="93.685" width="0.508" layer="16"/>
@@
 <wire x1="82.5" y1="48.76" x2="82.5" y2="45.2" width="0.508" layer="16"/>
 <wire x1="82.5" y1="45.2" x2="82.6" y2="45.1" width="0.508" layer="16"/>
+<wire x1="14.7" y1="93.42" x2="14.7" y2="87.755" width="0.508" layer="16"/>
+<wire x1="14.7" y1="87.755" x2="14.75" y2="87.705" width="0.508" layer="16"/>
 </signal>
 <signal name="VOUT">
